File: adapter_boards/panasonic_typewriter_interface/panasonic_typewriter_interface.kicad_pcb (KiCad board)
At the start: 2 copper layers, 37.2 x 45.7 mm, 28 parts, among them J1 KMDGX-8S-AS, J2 Conn_02x03_Odd_Even, J3 Conn_01x06_MountingPin, J4 Conn_01x06_MountingPin, J5 Conn_01x04_MountingPin, SW1 SW_SPDT, SW2 SW_Push

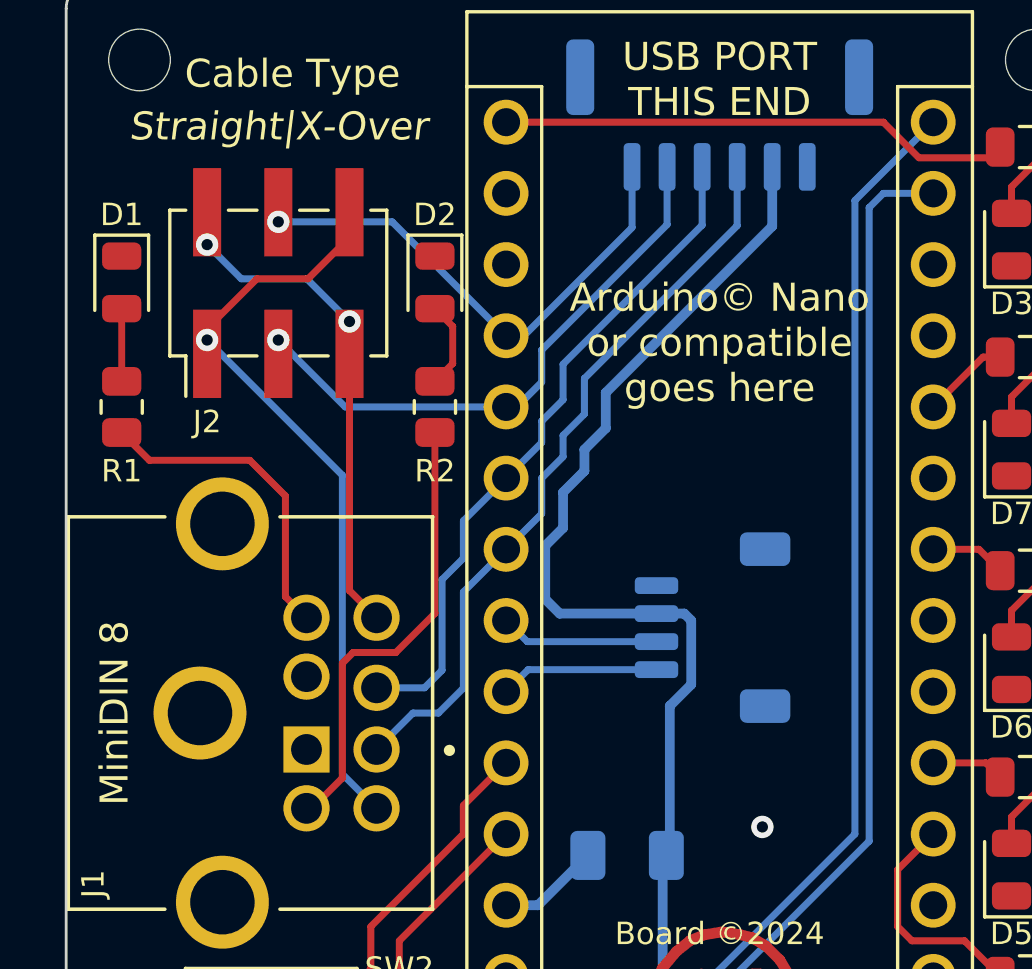
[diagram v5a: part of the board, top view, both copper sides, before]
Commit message: Convert to kicad 8; add space for qr code
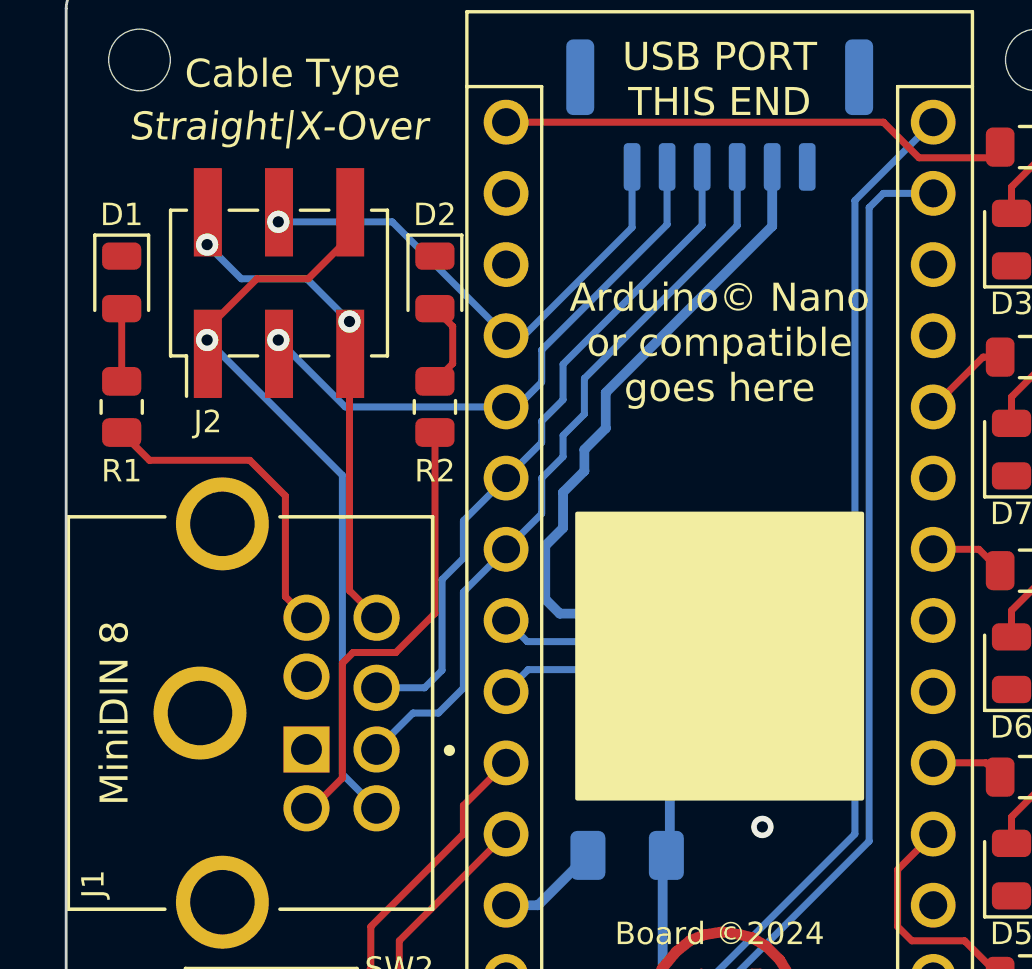
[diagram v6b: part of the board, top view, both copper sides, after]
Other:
- board text removed: "I routed +5V like this just to avoid extra vias!"
- board text removed: "I router +5V this way just to avoid using 4 more vias"
